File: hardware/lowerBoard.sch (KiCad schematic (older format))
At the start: 4 parts, among them K1 FINDER-34.51, U3 R-78B3.3-2.0

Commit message: replaced separated driver parts with driver chips and LED bars
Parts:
- renumbered U3 to U5
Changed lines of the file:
@@
 EESchema Schematic File Version 4
-LIBS:heating-control-cache
+LIBS:relays-device-cache
 EELAYER 30 0
 EELAYER END
 $Descr A4 11693 8268
 encoding utf-8
-Sheet 1 4
+Sheet 3 3
 Title ""
 Date ""
@@
 AR Path="/5DA00118" Ref="D1"  Part="1"
 AR Path="/5D9FF064/5DA00118" Ref="D3"  Part="1"
-F 0 "D1" V 3454 1879 50  0000 L CNN
+F 0 "D3" V 3454 1879 50  0000 L CNN
 F 1 "1N4148" V 3545 1879 50  0000 L CNN
 F 2 "Diode_THT:D_DO-35_SOD27_P7.62mm_Horizontal" H 3500 1625 50  0001 C CNN
@@
 AR Path="/5DA0011E" Ref="#PWR0102"  Part="1"
 AR Path="/5D9FF064/5DA0011E" Ref="#PWR0112"  Part="1"
-F 0 "#PWR0102" H 3950 1150 50  0001 C CNN
+F 0 "#PWR0112" H 3950 1150 50  0001 C CNN
 F 1 "+12V" H 3965 1473 50  0000 C CNN
 F 2 "" H 3950 1300 50  0001 C CNN
@@
 GND
 $Comp
-L Regulator_Switching:R-78B3.3-2.0 U3
+L Regulator_Switching:R-78B3.3-2.0 U5
 U 1 1 5DBF2EA9
 P 6950 1450
-F 0 "U3" H 6950 1692 50  0000 C CNN
+F 0 "U5" H 6950 1692 50  0000 C CNN
 F 1 "R-78B3.3-2.0" H 6950 1601 50  0000 C CNN
 F 2 "Converter_DCDC:Converter_DCDC_RECOM_R-78B-2.0_THT" H 7000 1200 50  0001 L CIN

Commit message: extracted relay to sub schematic to be able to multiply it
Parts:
- removed D1: 1N4148, Diode_THT:D_DO-35_SOD27_P7.62mm_Horizontal, symbol Diode:1N4148
- removed K1: FINDER-34.51, Relay_THT:Relay_SPDT_Finder_34.51_Vertical, symbol Relay:FINDER-34.51
- removed U5: R-78B3.3-2.0, Converter_DCDC:Converter_DCDC_RECOM_R-78B-2.0_THT, symbol Regulator_Switching:R-78B3.3-2.0
- added PS1: HLK-PM12, Converter_ACDC:Converter_ACDC_HiLink_HLK-PMxx, symbol Converter_ACDC:HLK-PM12
- added U3: R-783.3-0.5, Converter_DCDC:Converter_DCDC_RECOM_R-78E-0.5_THT, symbol Regulator_Switching:R-783.3-0.5
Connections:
- net labels added: 02, 12V
- net labels removed: +12V
- wire segments 22 -> 21
- no-connect marks 3 -> 2
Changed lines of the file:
@@
 $Descr A4 11693 8268
 encoding utf-8
-Sheet 3 3
+Sheet 3 5
 Title ""
 Date ""
@@
 Comment4 ""
 $EndDescr
-$Comp
-L Relay:FINDER-34.51 K1
-U 1 1 5DA00112
-P 4150 1800
-AR Path="/5DA00112" Ref="K1"  Part="1"
-AR Path="/5D9FF064/5DA00112" Ref="K1"  Part="1"
-F 0 "K1" H 4580 1846 50  0000 L CNN
-F 1 "FINDER-34.51" H 4580 1755 50  0000 L CNN
-F 2 "Relay_THT:Relay_SPDT_Finder_34.51_Vertical" H 5290 1760 50  0001 C CNN
-F 3 "https://gfinder.findernet.com/public/attachments/34/EN/S34USAEN.pdf" H 4150 1800 50  0001 C CNN
-	1    4150 1800
-	1    0    0    -1
-$EndComp
-$Comp
-L Diode:1N4148 D1
-U 1 1 5DA00118
-P 3500 1800
-AR Path="/5DA00118" Ref="D1"  Part="1"
-AR Path="/5D9FF064/5DA00118" Ref="D3"  Part="1"
-F 0 "D3" V 3454 1879 50  0000 L CNN
-F 1 "1N4148" V 3545 1879 50  0000 L CNN
-F 2 "Diode_THT:D_DO-35_SOD27_P7.62mm_Horizontal" H 3500 1625 50  0001 C CNN
-F 3 "https://assets.nexperia.com/documents/data-sheet/1N4148_1N4448.pdf" H 3500 1800 50  0001 C CNN
-	1    3500 1800
-	0    1    1    0
-$EndComp
-$Comp
-L power:+12V #PWR0102
-U 1 1 5DA0011E
-P 3950 1300
-AR Path="/5DA0011E" Ref="#PWR0102"  Part="1"
-AR Path="/5D9FF064/5DA0011E" Ref="#PWR0112"  Part="1"
-F 0 "#PWR0112" H 3950 1150 50  0001 C CNN
-F 1 "+12V" H 3965 1473 50  0000 C CNN
-F 2 "" H 3950 1300 50  0001 C CNN
-F 3 "" H 3950 1300 50  0001 C CNN
-	1    3950 1300
-	1    0    0    -1
-$EndComp
-Wire Wire Line
-	3950 1500 3950 1400
-Wire Wire Line
-	3500 1650 3500 1400
-Wire Wire Line
-	3500 1400 3950 1400
-Wire Wire Line
-	3500 1950 3500 2200
-Wire Wire Line
-	3500 2200 3950 2200
-Connection ~ 3950 2200
-Wire Wire Line
-	3950 2200 3950 2100
-NoConn ~ 4250 1500
-NoConn ~ 4450 1500
-NoConn ~ 4350 2100
-Wire Wire Line
-	3950 1300 3950 1400
-Connection ~ 3950 1400
 Text HLabel 8600 1450 2    50   UnSpc ~ 0
 3.3V
 Text HLabel 8600 1700 2    50   UnSpc ~ 0
 GND
-$Comp
-L Regulator_Switching:R-78B3.3-2.0 U5
-U 1 1 5DBF2EA9
-P 6950 1450
-F 0 "U5" H 6950 1692 50  0000 C CNN
-F 1 "R-78B3.3-2.0" H 6950 1601 50  0000 C CNN
-F 2 "Converter_DCDC:Converter_DCDC_RECOM_R-78B-2.0_THT" H 7000 1200 50  0001 L CIN
-F 3 "https://www.recom-power.com/pdf/Innoline/R-78Bxx-2.0.pdf" H 6950 1450 50  0001 C CNN
-	1    6950 1450
-	1    0    0    -1
-$EndComp
 Wire Wire Line
 	7250 1450 7650 1450
-$Comp
-L power:GND #PWR0101
-U 1 1 5DBF393B
-P 6950 2200
-F 0 "#PWR0101" H 6950 1950 50  0001 C CNN
-F 1 "GND" H 6955 2027 50  0000 C CNN
-F 2 "" H 6950 2200 50  0001 C CNN
-F 3 "" H 6950 2200 50  0001 C CNN
-	1    6950 2200
-	1    0    0    -1
-$EndComp
 Wire Wire Line
 	6950 1750 6950 1850
-Text HLabel 3200 2600 0    50   UnSpc ~ 0
+Text HLabel 1900 900  0    50   UnSpc ~ 0
 01
-Wire Wire Line
-	3950 2200 3950 2600
-Wire Wire Line
-	3200 2600 3950 2600
-Wire Wire Line
-	6650 1450 5650 1450
-Wire Wire Line
-	5650 1450 5650 1400
 Wire Wire Line
 	8600 1700 7900 1700
 Wire Wire Line
 	7900 1700 7900 1850
-Connection ~ 6950 1850
-Wire Wire Line
-	6950 1850 6950 2200
 Wire Wire Line
 	6950 1850 7650 1850
-Wire Wire Line
-	3950 1400 5650 1400
 $Comp
 L Device:CP C1
@@
 Wire Wire Line
 	7650 1850 7900 1850
+$Comp
+L Converter_ACDC:HLK-PM12 PS1
+U 1 1 5D9D8B1D
+P 5300 1200
+F 0 "PS1" H 5300 1525 50  0000 C CNN
+F 1 "HLK-PM12" H 5300 1434 50  0000 C CNN
+F 2 "Converter_ACDC:Converter_ACDC_HiLink_HLK-PMxx" H 5300 900 50  0001 C CNN
+F 3 "http://www.hlktech.net/product_detail.php?ProId=56" H 5700 850 50  0001 C CNN
+	1    5300 1200
+	1    0    0    -1
+$EndComp
+$Comp
+L Regulator_Switching:R-783.3-0.5 U3
+U 1 1 5D9DC2C0
+P 6950 1450
+F 0 "U3" H 6950 1692 50  0000 C CNN
+F 1 "R-783.3-0.5" H 6950 1601 50  0000 C CNN
+F 2 "Converter_DCDC:Converter_DCDC_RECOM_R-78E-0.5_THT" H 7000 1200 50  0001 L CIN
+F 3 "https://www.recom-power.com/pdf/Innoline/R-78xx-0.5.pdf" H 6950 1450 50  0001 C CNN
+	1    6950 1450
+	1    0    0    -1
+$EndComp
+Wire Wire Line
+	5700 1100 5800 1100
+Wire Wire Line
+	5800 1100 5800 1000
+Wire Wire Line
+	5700 1300 5800 1300
+Wire Wire Line
+	5800 1300 5800 1400
+NoConn ~ 4900 1100
+NoConn ~ 4900 1300
+Text HLabel 5800 1000 1    50   UnSpc ~ 0
+12V
+Text HLabel 5800 1400 3    50   UnSpc ~ 0
+GND
+Text HLabel 6550 1350 1    50   UnSpc ~ 0
+12V
+Wire Wire Line
+	6650 1450 6550 1450
+Wire Wire Line
+	6550 1450 6550 1350
+Wire Wire Line
+	1900 900  2050 900
+Text HLabel 1650 700  1    50   UnSpc ~ 0
+12V
+$Sheet
+S 2050 1200 550  200
+U 5D9F100B
+F0 "relais02" 50
+F1 "relais.sch" 50
+F2 "12V" U L 2050 1350 50
+F3 "in" U L 2050 1250 50
+$EndSheet
+Text HLabel 1900 1200 0    50   UnSpc ~ 0
+02
+Wire Wire Line
+	2050 1200 1900 1200
+$Sheet
+S 2050 850  550  200
+U 5D9EA18F
+F0 "relais01" 50
+F1 "relais.sch" 50
+F2 "12V" U L 2050 1000 50
+F3 "in" U L 2050 900 50
+$EndSheet
+Wire Wire Line
+	2050 1000 1650 1000
+Wire Wire Line
+	1650 1000 1650 700
+Wire Wire Line
+	2050 1350 1650 1350
+Wire Wire Line
+	1650 1350 1650 1000
+Connection ~ 1650 1000
 $EndSCHEMATC

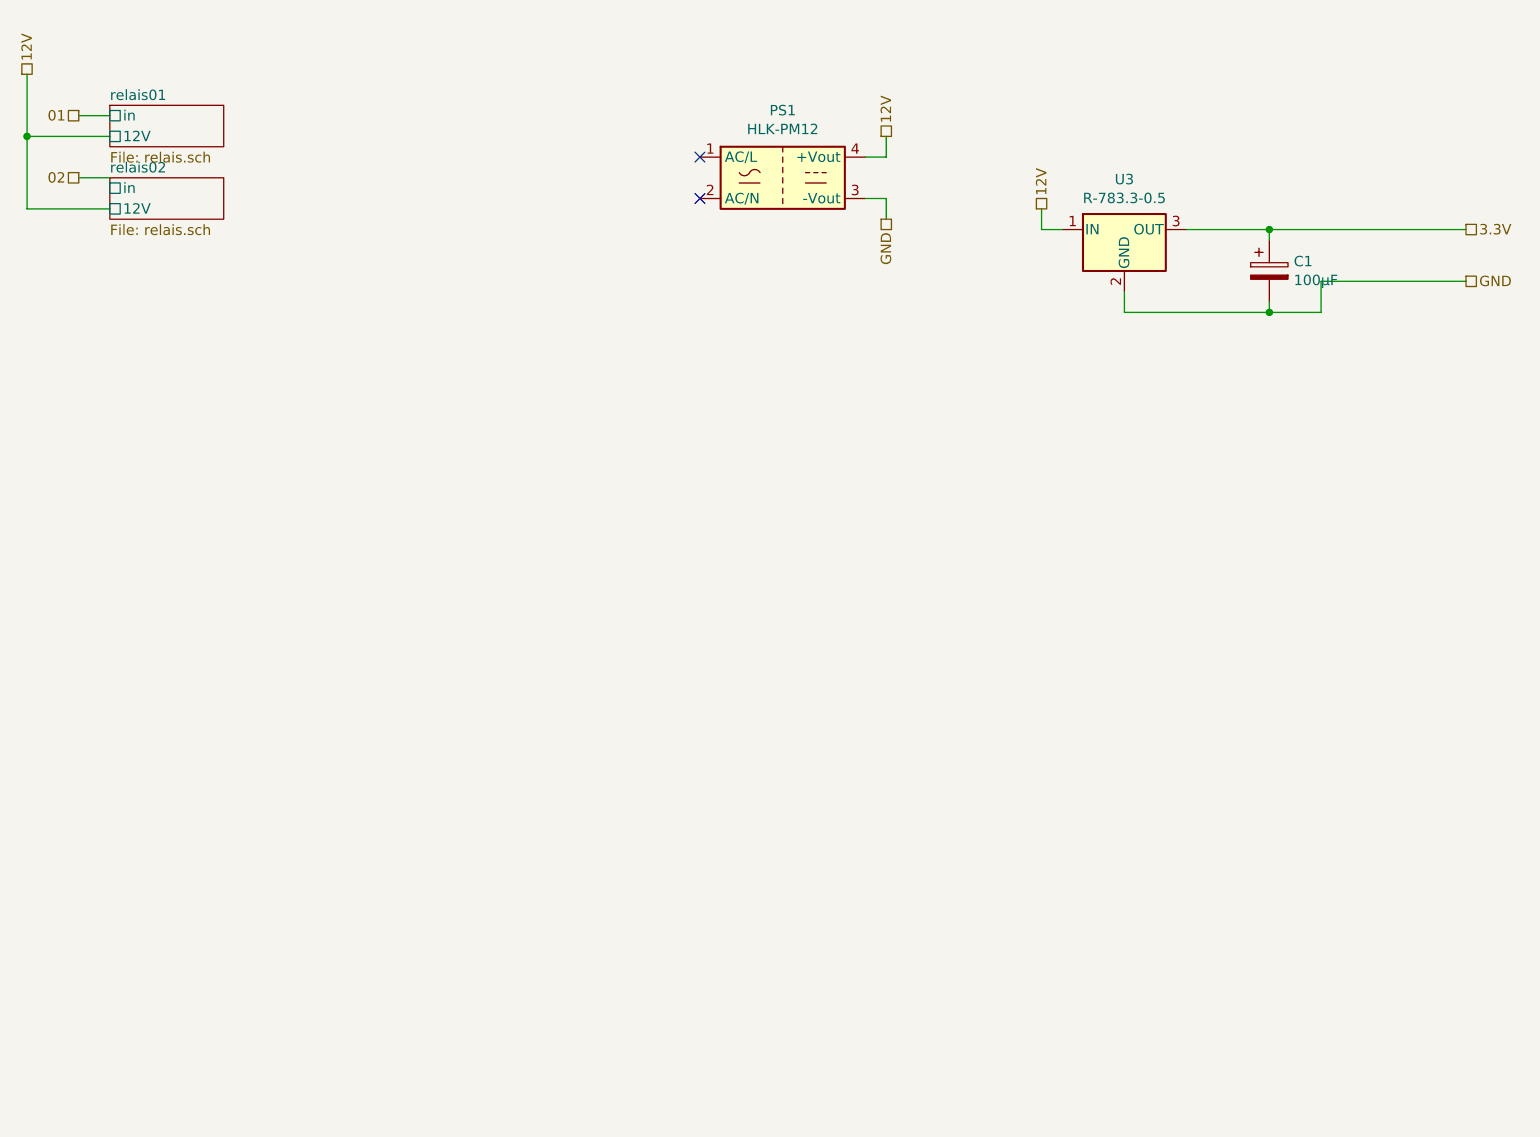
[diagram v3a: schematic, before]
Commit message: finished schematic mostly
started to create lower PCB
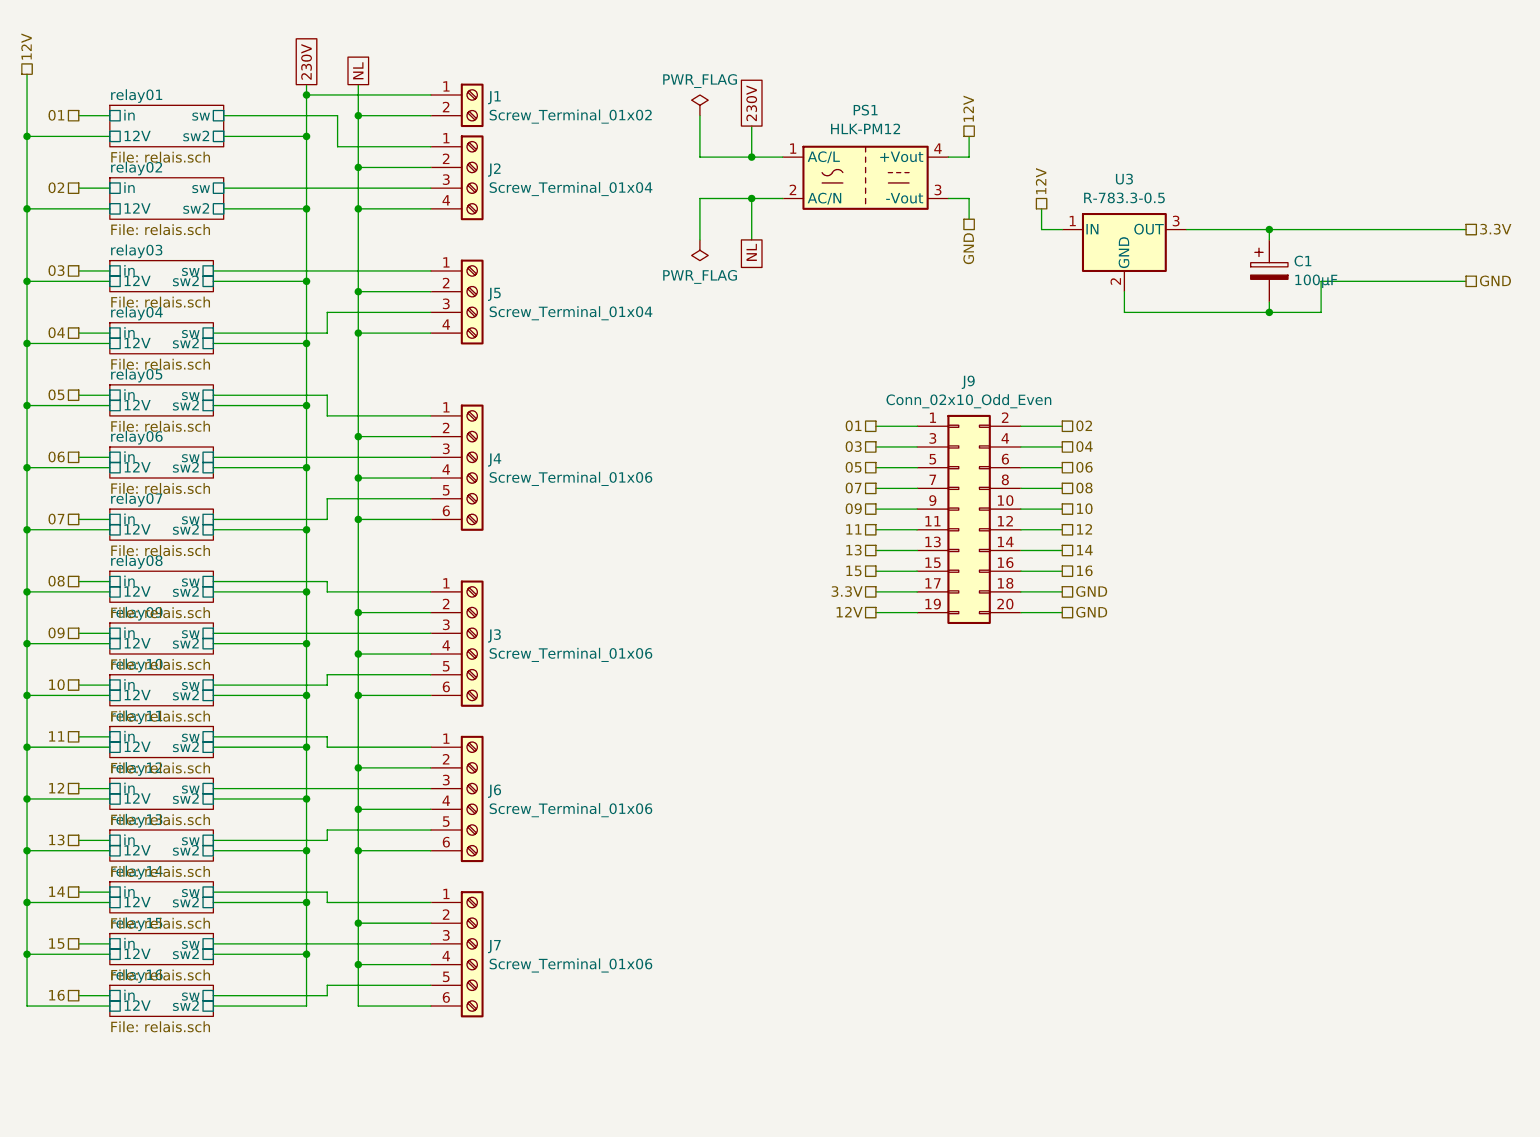
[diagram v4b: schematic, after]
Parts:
- added J1: Screw_Terminal_01x02, TerminalBlock_MetzConnect:TerminalBlock_MetzConnect_Type059_RT06302HBWC_1x02_P3.50mm_Horizontal, symbol Connector:Screw_Terminal_01x02
- added J2, J5: Screw_Terminal_01x04, TerminalBlock_MetzConnect:TerminalBlock_MetzConnect_Type059_RT06304HBWC_1x04_P3.50mm_Horizontal, symbol Connector:Screw_Terminal_01x04
- added J3, J4, J6, J7: Screw_Terminal_01x06, TerminalBlock_MetzConnect:TerminalBlock_MetzConnect_Type059_RT06306HBWC_1x06_P3.50mm_Horizontal, symbol Connector:Screw_Terminal_01x06
- added J9: Conn_02x10_Odd_Even, Connector_PinHeader_2.54mm:PinHeader_2x10_P2.54mm_Vertical, symbol Connector_Generic:Conn_02x10_Odd_Even
- C1: footprint (none) -> Capacitor_THT:CP_Radial_D6.3mm_P2.50mm
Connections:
- net labels added: 03, 04, 05, 06, 07, 08, 09, 10, 11, 12, 13, 14, 15, 16, 230V, NL
- wire segments 21 -> 195
- no-connect marks 2 -> 0
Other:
- moved on the sheet: PS1

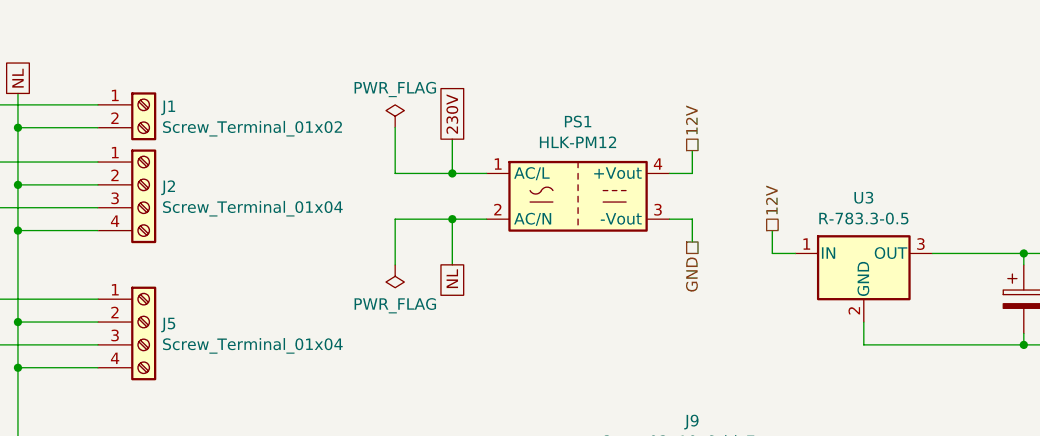
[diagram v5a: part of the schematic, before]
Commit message: replaced MCP23016 with MCP23017
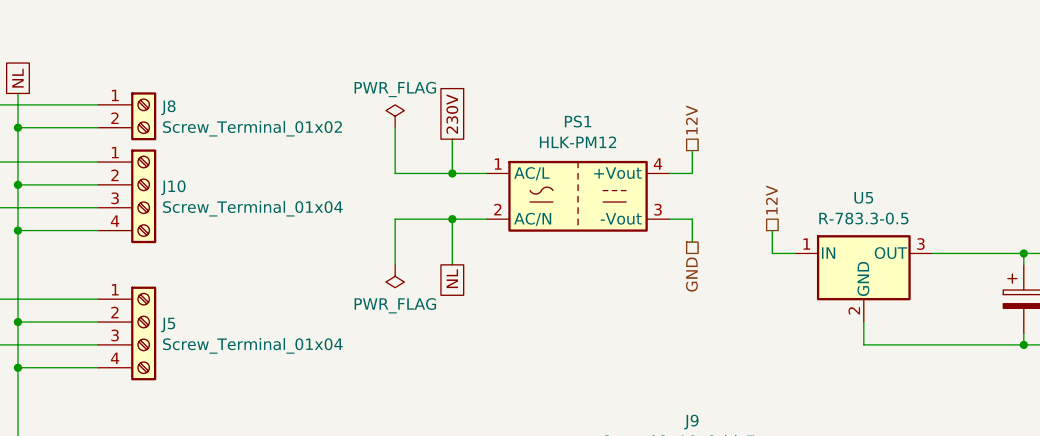
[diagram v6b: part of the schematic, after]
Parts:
- renumbered J2 to J10, J1 to J8, U3 to U5
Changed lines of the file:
@@
 $Descr A4 11693 8268
 encoding utf-8
-Sheet 1 19
+Sheet 3 19
 Title ""
 Date ""
@@
 $EndComp
 $Comp
-L Regulator_Switching:R-783.3-0.5 U3
+L Regulator_Switching:R-783.3-0.5 U5
 U 1 1 5D9DC2C0
 P 6950 1450
-F 0 "U3" H 6950 1692 50  0000 C CNN
+F 0 "U5" H 6950 1692 50  0000 C CNN
 F 1 "R-783.3-0.5" H 6950 1601 50  0000 C CNN
 F 2 "Converter_DCDC:Converter_DCDC_RECOM_R-78E-0.5_THT" H 7000 1200 50  0001 L CIN
@@
 	3250 2850 3250 3300
 $Comp
-L Connector:Screw_Terminal_01x02 J1
+L Connector:Screw_Terminal_01x02 J8
 U 1 1 5DC094BA
 P 3800 800
-F 0 "J1" H 3880 792 50  0000 L CNN
+F 0 "J8" H 3880 792 50  0000 L CNN
 F 1 "Screw_Terminal_01x02" H 3880 701 50  0000 L CNN
 F 2 "TerminalBlock_MetzConnect:TerminalBlock_MetzConnect_Type059_RT06302HBWC_1x02_P3.50mm_Horizontal" H 3800 800 50  0001 C CNN
@@
 	3250 1950 3250 2450
 $Comp
-L Connector:Screw_Terminal_01x04 J2
+L Connector:Screw_Terminal_01x04 J10
 U 1 1 5DC67C79
 P 3800 1150
-F 0 "J2" H 3880 1142 50  0000 L CNN
+F 0 "J10" H 3880 1142 50  0000 L CNN
 F 1 "Screw_Terminal_01x04" H 3880 1051 50  0000 L CNN
 F 2 "TerminalBlock_MetzConnect:TerminalBlock_MetzConnect_Type059_RT06304HBWC_1x04_P3.50mm_Horizontal" H 3800 1150 50  0001 C CNN

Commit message: lower board fixes and started with upper printed circuit board
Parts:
- removed J10, J5: Screw_Terminal_01x04, TerminalBlock_MetzConnect:TerminalBlock_MetzConnect_Type059_RT06304HBWC_1x04_P3.50mm_Horizontal, symbol Connector:Screw_Terminal_01x04
- removed J3, J4, J6, J7: Screw_Terminal_01x06, TerminalBlock_MetzConnect:TerminalBlock_MetzConnect_Type059_RT06306HBWC_1x06_P3.50mm_Horizontal, symbol Connector:Screw_Terminal_01x06
- added J10, J11, J12, J13, J14, J15, J16, J17, J18, J19, J20, J3, J4, J5, J6, J7: Screw_Terminal_01x02, TerminalBlock_MetzConnect:TerminalBlock_MetzConnect_Type059_RT06302HBWC_1x02_P3.50mm_Horizontal, symbol Connector:Screw_Terminal_01x02
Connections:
- net relay01/sw: now also J3.1 (Pin_1)
- net relay02/sw: now also J4.1 (Pin_1)
- net relay03/sw: now also J5.1 (Pin_1)
- net relay04/sw: now also J6.1 (Pin_1)
- net relay05/sw: now also J7.1 (Pin_1)
- net relay06/sw: now also J10.1 (Pin_1)
- net relay07/sw: now also J11.1 (Pin_1)
- net relay08/sw: now also J12.1 (Pin_1)
- net relay09/sw: now also J13.1 (Pin_1)
- net relay10/sw: now also J14.1 (Pin_1)
- net relay11/sw: now also J15.1 (Pin_1)
- net relay12/sw: now also J16.1 (Pin_1)
- net relay13/sw: now also J17.1 (Pin_1)
- net relay14/sw: now also J18.1 (Pin_1)
- net relay15/sw: now also J19.1 (Pin_1)
- net relay16/sw: now also J20.1 (Pin_1)
- net 230V: no longer names the net of PS1.1 (AC/L)
- net 230V: now also J8.2 (Pin_2); no longer J8.1 (Pin_1)
- net NL: no longer names the net of PS1.2 (AC/N)
- net NL: now also J8.1 (Pin_1); no longer J8.2 (Pin_2)
- new net relay01/sw2: J3.2 (Pin_2)
- new net relay02/sw2: J4.2 (Pin_2)
- new net relay03/sw2: J5.2 (Pin_2)
- new net relay04/sw2: J6.2 (Pin_2)
- new net relay05/sw2: J7.2 (Pin_2)
- new net relay06/sw2: J10.2 (Pin_2)
- new net relay07/sw2: J11.2 (Pin_2)
- new net relay08/sw2: J12.2 (Pin_2)
- new net relay09/sw2: J13.2 (Pin_2)
- new net relay10/sw2: J14.2 (Pin_2)
- new net relay11/sw2: J15.2 (Pin_2)
- new net relay12/sw2: J16.2 (Pin_2)
- new net relay13/sw2: J17.2 (Pin_2)
- new net relay14/sw2: J18.2 (Pin_2)
- new net relay15/sw2: J19.2 (Pin_2)
- new net relay16/sw2: J20.2 (Pin_2)
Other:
- moved on the sheet: C1, J8, PS1, U5
